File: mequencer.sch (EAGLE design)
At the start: 75 parts, among them IC1 NE555D, IC10 LF353D, IC11 NE555D, IC12 NE555D, IC2 4163D, IC3 74HC85D, IC4 4051D, IC5 4051D, IC6 74HCT04D, IC7 4051D, IC8 4051D, IC9 LF353D, U1 74LVC1G08SE-7

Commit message: Moving shit around more
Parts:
- removed C20, C21, C22, C23, C24, C25: .1uF, SparkFun-Capacitors:CAP0603-CAP
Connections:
- net 5V: no longer C20.2, C21.2, C22.2, C23.2, C24.2, C25.2
- net N$7: no longer C20.1, C21.1, C22.1, C23.1, C24.1, C25.1
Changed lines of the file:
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@@
 <part name="C18" library="SparkFun-Capacitors" deviceset="CAP" device="0603-CAP" value=".1uF"/>
 <part name="C19" library="SparkFun-Capacitors" deviceset="CAP" device="0603-CAP" value=".1uF"/>
-<part name="C20" library="SparkFun-Capacitors" deviceset="CAP" device="0603-CAP" value=".1uF"/>
-<part name="C21" library="SparkFun-Capacitors" deviceset="CAP" device="0603-CAP" value=".1uF"/>
-<part name="C22" library="SparkFun-Capacitors" deviceset="CAP" device="0603-CAP" value=".1uF"/>
-<part name="C23" library="SparkFun-Capacitors" deviceset="CAP" device="0603-CAP" value=".1uF"/>
-<part name="C24" library="SparkFun-Capacitors" deviceset="CAP" device="0603-CAP" value=".1uF"/>
-<part name="C25" library="SparkFun-Capacitors" deviceset="CAP" device="0603-CAP" value=".1uF"/>
 <part name="R2" library="SparkFun-Resistors" deviceset="RESISTOR" device="0603" value="1k"/>
 <part name="JP2" library="SparkFun-Connectors" deviceset="M04" device="JST-PTH"/>
@@
 <instance part="C5" gate="G$1" x="26.67" y="173.99" rot="R180"/>
 <instance part="C6" gate="G$1" x="55.88" y="172.72" rot="R180"/>
-<instance part="SUPPLY13" gate="G$1" x="92.71" y="181.61"/>
+<instance part="SUPPLY13" gate="G$1" x="128.27" y="184.15"/>
 <instance part="GND4" gate="1" x="237.49" y="100.33"/>
 <instance part="C7" gate="G$1" x="156.21" y="180.34" rot="R180"/>
@@
 <instance part="C18" gate="G$1" x="135.89" y="180.34" rot="R180"/>
 <instance part="C19" gate="G$1" x="130.81" y="180.34" rot="R180"/>
-<instance part="C20" gate="G$1" x="125.73" y="180.34" rot="R180"/>
-<instance part="C21" gate="G$1" x="120.65" y="180.34" rot="R180"/>
-<instance part="C22" gate="G$1" x="115.57" y="180.34" rot="R180"/>
-<instance part="C23" gate="G$1" x="110.49" y="180.34" rot="R180"/>
-<instance part="C24" gate="G$1" x="105.41" y="180.34" rot="R180"/>
-<instance part="C25" gate="G$1" x="100.33" y="180.34" rot="R180"/>
 <instance part="R2" gate="G$1" x="25.4" y="149.86"/>
 <instance part="JP2" gate="G$1" x="10.16" y="-15.24"/>
@@
 </segment>
 <segment>
-<pinref part="C25" gate="G$1" pin="2"/>
-<pinref part="C24" gate="G$1" pin="2"/>
-<wire x1="100.33" y1="182.88" x2="105.41" y2="182.88" width="0.1524" layer="91"/>
-<pinref part="C23" gate="G$1" pin="2"/>
-<wire x1="105.41" y1="182.88" x2="110.49" y2="182.88" width="0.1524" layer="91"/>
-<junction x="105.41" y="182.88"/>
-<pinref part="C22" gate="G$1" pin="2"/>
-<wire x1="110.49" y1="182.88" x2="115.57" y2="182.88" width="0.1524" layer="91"/>
-<junction x="110.49" y="182.88"/>
-<pinref part="C21" gate="G$1" pin="2"/>
-<wire x1="115.57" y1="182.88" x2="120.65" y2="182.88" width="0.1524" layer="91"/>
-<junction x="115.57" y="182.88"/>
-<pinref part="C20" gate="G$1" pin="2"/>
-<wire x1="120.65" y1="182.88" x2="125.73" y2="182.88" width="0.1524" layer="91"/>
-<junction x="120.65" y="182.88"/>
 <pinref part="C19" gate="G$1" pin="2"/>
-<wire x1="125.73" y1="182.88" x2="130.81" y2="182.88" width="0.1524" layer="91"/>
-<junction x="125.73" y="182.88"/>
+<wire x1="128.27" y1="182.88" x2="130.81" y2="182.88" width="0.1524" layer="91"/>
 <pinref part="C18" gate="G$1" pin="2"/>
 <wire x1="130.81" y1="182.88" x2="135.89" y2="182.88" width="0.1524" layer="91"/>
@@
 <junction x="186.69" y="182.88"/>
 <pinref part="SUPPLY13" gate="G$1" pin="5V"/>
-<wire x1="100.33" y1="182.88" x2="92.71" y2="182.88" width="0.1524" layer="91"/>
-<wire x1="92.71" y1="182.88" x2="92.71" y2="181.61" width="0.1524" layer="91"/>
-<junction x="100.33" y="182.88"/>
+<wire x1="128.27" y1="182.88" x2="128.27" y2="184.15" width="0.1524" layer="91"/>
 </segment>
 <segment>
@@
 <wire x1="208.28" y1="124.46" x2="223.52" y2="124.46" width="0.1524" layer="91"/>
 <junction x="223.52" y="124.46"/>
-<pinref part="C25" gate="G$1" pin="1"/>
-<pinref part="C24" gate="G$1" pin="1"/>
-<wire x1="100.33" y1="175.26" x2="105.41" y2="175.26" width="0.1524" layer="91"/>
-<pinref part="C23" gate="G$1" pin="1"/>
-<wire x1="105.41" y1="175.26" x2="110.49" y2="175.26" width="0.1524" layer="91"/>
-<junction x="105.41" y="175.26"/>
-<pinref part="C22" gate="G$1" pin="1"/>
-<wire x1="110.49" y1="175.26" x2="115.57" y2="175.26" width="0.1524" layer="91"/>
-<junction x="110.49" y="175.26"/>
-<pinref part="C21" gate="G$1" pin="1"/>
-<wire x1="115.57" y1="175.26" x2="120.65" y2="175.26" width="0.1524" layer="91"/>
-<junction x="115.57" y="175.26"/>
-<pinref part="C20" gate="G$1" pin="1"/>
-<wire x1="120.65" y1="175.26" x2="125.73" y2="175.26" width="0.1524" layer="91"/>
-<junction x="120.65" y="175.26"/>
 <pinref part="C19" gate="G$1" pin="1"/>
-<wire x1="125.73" y1="175.26" x2="130.81" y2="175.26" width="0.1524" layer="91"/>
-<junction x="125.73" y="175.26"/>
 <pinref part="C18" gate="G$1" pin="1"/>
 <wire x1="130.81" y1="175.26" x2="135.89" y2="175.26" width="0.1524" layer="91"/>
-<junction x="130.81" y="175.26"/>
 <pinref part="C17" gate="G$1" pin="1"/>
 <wire x1="135.89" y1="175.26" x2="140.97" y2="175.26" width="0.1524" layer="91"/>

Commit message: stuff
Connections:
- removed net N$7: C10.1, C11.1, C12.1, C13.1, C14.1, C15.1, C16.1, C17.1, C18.1, C19.1, C7.1, C8.1, C9.1, IC10P.V+, IC2P.VDD, IC3P.VCC, IC4P.VCC, IC5P.VCC, IC6P.VCC, IC7P.VCC, IC8P.VCC, IC9P.V+
- net 5V: now also IC10P.V+, IC2P.VDD, IC3P.VCC, IC4P.VCC, IC5P.VCC, IC6P.VCC, IC7P.VCC, IC8P.VCC, IC9P.V+
- net GND: now also C10.1, C11.1, C12.1, C13.1, C14.1, C15.1, C16.1, C17.1, C18.1, C19.1, C7.1, C8.1, C9.1
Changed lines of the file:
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@@
 <setting verticaltext="up"/>
 </settings>
-<grid distance="0.1" unitdist="inch" unit="inch" style="lines" multiple="1" display="no" altdistance="0.01" altunitdist="inch" altunit="inch"/>
+<grid distance="0.05" unitdist="inch" unit="inch" style="lines" multiple="1" display="yes" altdistance="0.005" altunitdist="inch" altunit="inch"/>
 <layers>
 <layer number="1" name="Top" color="4" fill="1" visible="no" active="no"/>
@@
 <part name="SUPPLY29" library="SparkFun-Aesthetics" deviceset="5V" device=""/>
 <part name="GND3" library="SparkFun-Aesthetics" deviceset="GND" device=""/>
+<part name="GND5" library="SparkFun-Aesthetics" deviceset="GND" device=""/>
+<part name="SUPPLY4" library="SparkFun-Aesthetics" deviceset="5V" device=""/>
 </parts>
 <sheets>
@@
 <instance part="SUPPLY29" gate="G$1" x="78.74" y="114.3"/>
 <instance part="GND3" gate="1" x="101.6" y="88.9"/>
+<instance part="GND5" gate="1" x="191.77" y="171.45"/>
+<instance part="SUPPLY4" gate="G$1" x="208.28" y="177.8"/>
 </instances>
 <busses>
@@
 <pinref part="SUPPLY29" gate="G$1" pin="5V"/>
 </segment>
+<segment>
+<pinref part="IC8" gate="P" pin="VCC"/>
+<pinref part="IC10" gate="P" pin="V+"/>
+<wire x1="233.68" y1="124.46" x2="223.52" y2="124.46" width="0.1524" layer="91"/>
+<wire x1="208.28" y1="124.46" x2="223.52" y2="124.46" width="0.1524" layer="91"/>
+<junction x="223.52" y="124.46"/>
+<pinref part="IC9" gate="P" pin="V+"/>
+<wire x1="208.28" y1="177.8" x2="215.9" y2="177.8" width="0.1524" layer="91"/>
+<pinref part="IC3" gate="P" pin="VCC"/>
+<wire x1="226.06" y1="177.8" x2="215.9" y2="177.8" width="0.1524" layer="91"/>
+<junction x="215.9" y="177.8"/>
+<pinref part="IC2" gate="P" pin="VDD"/>
+<wire x1="226.06" y1="177.8" x2="233.68" y2="177.8" width="0.1524" layer="91"/>
+<junction x="226.06" y="177.8"/>
+<pinref part="IC4" gate="P" pin="VCC"/>
+<pinref part="IC5" gate="P" pin="VCC"/>
+<wire x1="233.68" y1="160.02" x2="220.98" y2="160.02" width="0.1524" layer="91"/>
+<wire x1="220.98" y1="160.02" x2="208.28" y2="160.02" width="0.1524" layer="91"/>
+<junction x="220.98" y="160.02"/>
+<wire x1="208.28" y1="177.8" x2="208.28" y2="160.02" width="0.1524" layer="91"/>
+<pinref part="IC6" gate="P" pin="VCC"/>
+<pinref part="IC7" gate="P" pin="VCC"/>
+<wire x1="233.68" y1="142.24" x2="226.06" y2="142.24" width="0.1524" layer="91"/>
+<wire x1="226.06" y1="142.24" x2="208.28" y2="142.24" width="0.1524" layer="91"/>
+<junction x="226.06" y="142.24"/>
+<wire x1="208.28" y1="160.02" x2="208.28" y2="142.24" width="0.1524" layer="91"/>
+<junction x="208.28" y="160.02"/>
+<wire x1="208.28" y1="124.46" x2="208.28" y2="142.24" width="0.1524" layer="91"/>
+<junction x="208.28" y="142.24"/>
+<pinref part="SUPPLY4" gate="G$1" pin="5V"/>
+<junction x="208.28" y="177.8"/>
+</segment>
 </net>
 <net name="GND" class="0">
@@
 <wire x1="101.6" y1="91.44" x2="96.52" y2="91.44" width="0.1524" layer="91"/>
 </segment>
+<segment>
+<pinref part="C16" gate="G$1" pin="1"/>
+<pinref part="C15" gate="G$1" pin="1"/>
+<wire x1="186.69" y1="175.26" x2="191.77" y2="175.26" width="0.1524" layer="91"/>
+<junction x="186.69" y="175.26"/>
+<pinref part="C14" gate="G$1" pin="1"/>
+<wire x1="181.61" y1="175.26" x2="186.69" y2="175.26" width="0.1524" layer="91"/>
+<junction x="181.61" y="175.26"/>
+<pinref part="C11" gate="G$1" pin="1"/>
+<wire x1="176.53" y1="175.26" x2="181.61" y2="175.26" width="0.1524" layer="91"/>
+<junction x="176.53" y="175.26"/>
+<pinref part="C10" gate="G$1" pin="1"/>
+<wire x1="171.45" y1="175.26" x2="176.53" y2="175.26" width="0.1524" layer="91"/>
+<junction x="171.45" y="175.26"/>
+<pinref part="C9" gate="G$1" pin="1"/>
+<wire x1="166.37" y1="175.26" x2="171.45" y2="175.26" width="0.1524" layer="91"/>
+<junction x="166.37" y="175.26"/>
+<pinref part="C8" gate="G$1" pin="1"/>
+<wire x1="161.29" y1="175.26" x2="166.37" y2="175.26" width="0.1524" layer="91"/>
+<junction x="161.29" y="175.26"/>
+<pinref part="C7" gate="G$1" pin="1"/>
+<wire x1="156.21" y1="175.26" x2="161.29" y2="175.26" width="0.1524" layer="91"/>
+<junction x="156.21" y="175.26"/>
+<pinref part="C12" gate="G$1" pin="1"/>
+<wire x1="151.13" y1="175.26" x2="156.21" y2="175.26" width="0.1524" layer="91"/>
+<junction x="151.13" y="175.26"/>
+<pinref part="C13" gate="G$1" pin="1"/>
+<wire x1="146.05" y1="175.26" x2="151.13" y2="175.26" width="0.1524" layer="91"/>
+<junction x="146.05" y="175.26"/>
+<pinref part="C17" gate="G$1" pin="1"/>
+<wire x1="140.97" y1="175.26" x2="146.05" y2="175.26" width="0.1524" layer="91"/>
+<junction x="140.97" y="175.26"/>
+<pinref part="C18" gate="G$1" pin="1"/>
+<wire x1="135.89" y1="175.26" x2="140.97" y2="175.26" width="0.1524" layer="91"/>
+<junction x="135.89" y="175.26"/>
+<pinref part="C19" gate="G$1" pin="1"/>
+<wire x1="130.81" y1="175.26" x2="135.89" y2="175.26" width="0.1524" layer="91"/>
+<pinref part="GND5" gate="1" pin="GND"/>
+<wire x1="191.77" y1="175.26" x2="191.77" y2="173.99" width="0.2032" layer="91"/>
+</segment>
 </net>
 <net name="N$2" class="0">
@@
 </segment>
 </net>
-<net name="N$7" class="0">
-<segment>
-<pinref part="IC8" gate="P" pin="VCC"/>
-<pinref part="IC10" gate="P" pin="V+"/>
-<wire x1="233.68" y1="124.46" x2="223.52" y2="124.46" width="0.1524" layer="91"/>
-<wire x1="208.28" y1="124.46" x2="223.52" y2="124.46" width="0.1524" layer="91"/>
-<junction x="223.52" y="124.46"/>
-<pinref part="C19" gate="G$1" pin="1"/>
-<pinref part="C18" gate="G$1" pin="1"/>
-<wire x1="130.81" y1="175.26" x2="135.89" y2="175.26" width="0.1524" layer="91"/>
-<pinref part="C17" gate="G$1" pin="1"/>
-<wire x1="135.89" y1="175.26" x2="140.97" y2="175.26" width="0.1524" layer="91"/>
-<junction x="135.89" y="175.26"/>
-<pinref part="C13" gate="G$1" pin="1"/>
-<wire x1="140.97" y1="175.26" x2="146.05" y2="175.26" width="0.1524" layer="91"/>
-<junction x="140.97" y="175.26"/>
-<pinref part="C12" gate="G$1" pin="1"/>
-<wire x1="146.05" y1="175.26" x2="151.13" y2="175.26" width="0.1524" layer="91"/>
-<junction x="146.05" y="175.26"/>
-<pinref part="C7" gate="G$1" pin="1"/>
-<wire x1="151.13" y1="175.26" x2="156.21" y2="175.26" width="0.1524" layer="91"/>
-<junction x="151.13" y="175.26"/>
-<pinref part="C8" gate="G$1" pin="1"/>
-<wire x1="156.21" y1="175.26" x2="161.29" y2="175.26" width="0.1524" layer="91"/>
-<junction x="156.21" y="175.26"/>
-<pinref part="C9" gate="G$1" pin="1"/>
-<wire x1="161.29" y1="175.26" x2="166.37" y2="175.26" width="0.1524" layer="91"/>
-<junction x="161.29" y="175.26"/>
-<pinref part="C10" gate="G$1" pin="1"/>
-<wire x1="166.37" y1="175.26" x2="171.45" y2="175.26" width="0.1524" layer="91"/>
-<junction x="166.37" y="175.26"/>
-<pinref part="C11" gate="G$1" pin="1"/>
-<wire x1="171.45" y1="175.26" x2="176.53" y2="175.26" width="0.1524" layer="91"/>
-<junction x="171.45" y="175.26"/>
-<pinref part="C14" gate="G$1" pin="1"/>
-<wire x1="176.53" y1="175.26" x2="181.61" y2="175.26" width="0.1524" layer="91"/>
-<junction x="176.53" y="175.26"/>
-<pinref part="C15" gate="G$1" pin="1"/>
-<wire x1="181.61" y1="175.26" x2="186.69" y2="175.26" width="0.1524" layer="91"/>
-<junction x="181.61" y="175.26"/>
-<pinref part="C16" gate="G$1" pin="1"/>
-<wire x1="186.69" y1="175.26" x2="191.77" y2="175.26" width="0.1524" layer="91"/>
-<junction x="186.69" y="175.26"/>
-<junction x="191.77" y="175.26"/>
-<wire x1="191.77" y1="175.26" x2="208.28" y2="175.26" width="0.1524" layer="91"/>
-<wire x1="208.28" y1="175.26" x2="208.28" y2="177.8" width="0.1524" layer="91"/>
-<pinref part="IC9" gate="P" pin="V+"/>
-<wire x1="208.28" y1="177.8" x2="215.9" y2="177.8" width="0.1524" layer="91"/>
-<pinref part="IC3" gate="P" pin="VCC"/>
-<wire x1="226.06" y1="177.8" x2="215.9" y2="177.8" width="0.1524" layer="91"/>
-<junction x="215.9" y="177.8"/>
-<pinref part="IC2" gate="P" pin="VDD"/>
-<wire x1="226.06" y1="177.8" x2="233.68" y2="177.8" width="0.1524" layer="91"/>
-<junction x="226.06" y="177.8"/>
-<pinref part="IC4" gate="P" pin="VCC"/>
-<pinref part="IC5" gate="P" pin="VCC"/>
-<wire x1="233.68" y1="160.02" x2="220.98" y2="160.02" width="0.1524" layer="91"/>
-<wire x1="220.98" y1="160.02" x2="208.28" y2="160.02" width="0.1524" layer="91"/>
-<junction x="220.98" y="160.02"/>
-<wire x1="208.28" y1="175.26" x2="208.28" y2="160.02" width="0.1524" layer="91"/>
-<junction x="208.28" y="175.26"/>
-<pinref part="IC6" gate="P" pin="VCC"/>
-<pinref part="IC7" gate="P" pin="VCC"/>
-<wire x1="233.68" y1="142.24" x2="226.06" y2="142.24" width="0.1524" layer="91"/>
-<wire x1="226.06" y1="142.24" x2="208.28" y2="142.24" width="0.1524" layer="91"/>
-<junction x="226.06" y="142.24"/>
-<wire x1="208.28" y1="160.02" x2="208.28" y2="142.24" width="0.1524" layer="91"/>
-<junction x="208.28" y="160.02"/>
-<wire x1="208.28" y1="124.46" x2="208.28" y2="142.24" width="0.1524" layer="91"/>
-<junction x="208.28" y="142.24"/>
-</segment>
-</net>

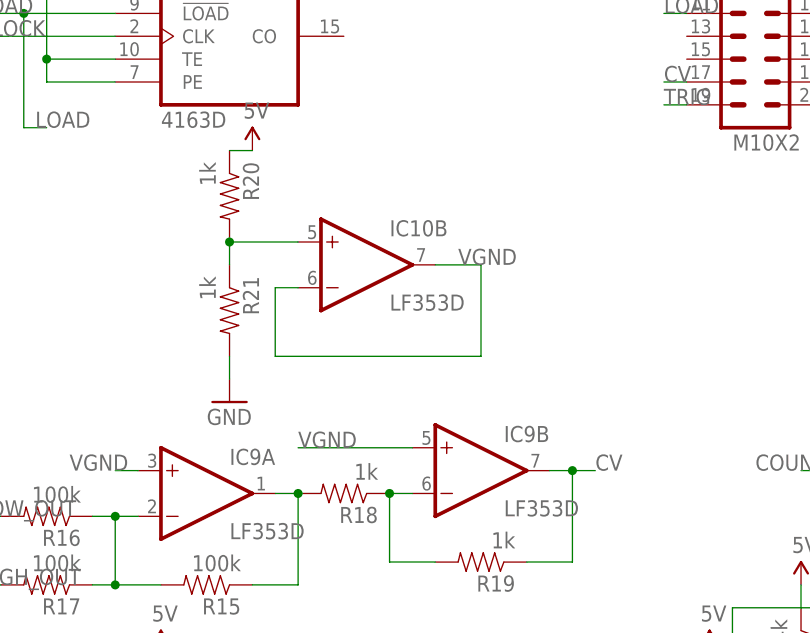
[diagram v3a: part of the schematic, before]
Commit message: changed some 1ks to 100ks to draw less current
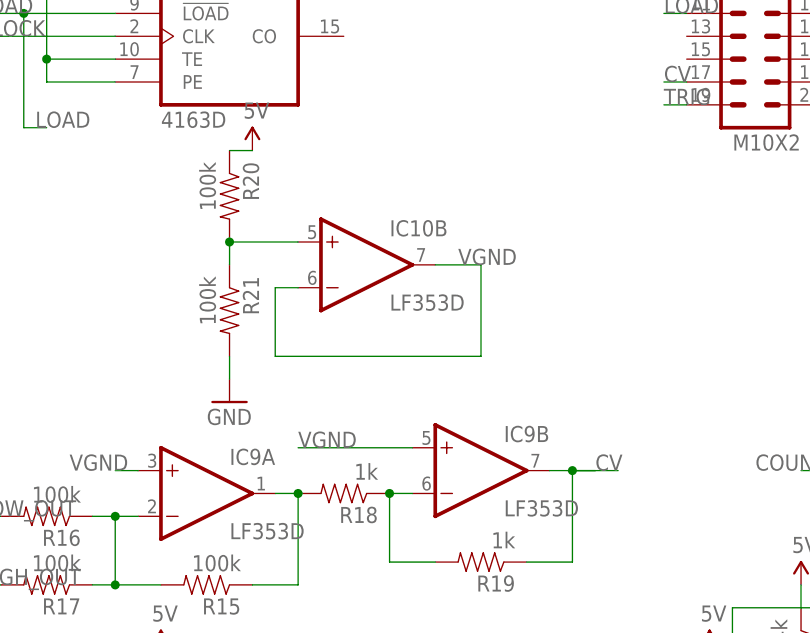
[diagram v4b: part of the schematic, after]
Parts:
- R20, R21: value 1k -> 100k
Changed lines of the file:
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@@
 <part name="R19" library="SparkFun-Resistors" deviceset="RESISTOR" device="0603" value="1k"/>
 <part name="IC10" library="linear" deviceset="LF353" device="D"/>
-<part name="R20" library="SparkFun-Resistors" deviceset="RESISTOR" device="0603" value="1k"/>
-<part name="R21" library="SparkFun-Resistors" deviceset="RESISTOR" device="0603" value="1k"/>
+<part name="R20" library="SparkFun-Resistors" deviceset="RESISTOR" device="0603" value="100k"/>
+<part name="R21" library="SparkFun-Resistors" deviceset="RESISTOR" device="0603" value="100k"/>
 <part name="GND10" library="SparkFun-Aesthetics" deviceset="GND" device=""/>
 <part name="SUPPLY7" library="SparkFun-Aesthetics" deviceset="5V" device=""/>
@@
 <junction x="68.58" y="50.8"/>
 <label x="71.12" y="50.8" size="1.778" layer="95"/>
-</segment>
-<segment>
+<wire x1="73.66" y1="50.8" x2="68.58" y2="50.8" width="0.1524" layer="91"/>
+</segment>
+<segment>

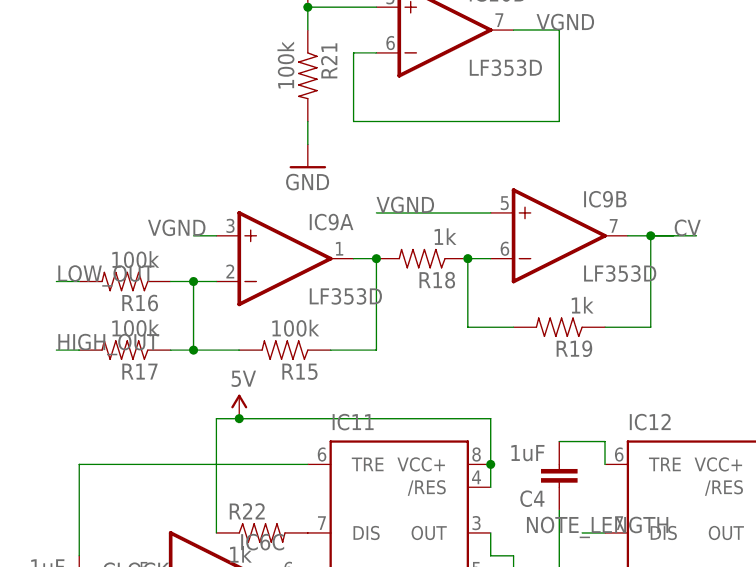
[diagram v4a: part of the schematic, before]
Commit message: bumped the resistance values in the CV summer so that the resistance in note pot won't affect the note's CV when it is in rest mode
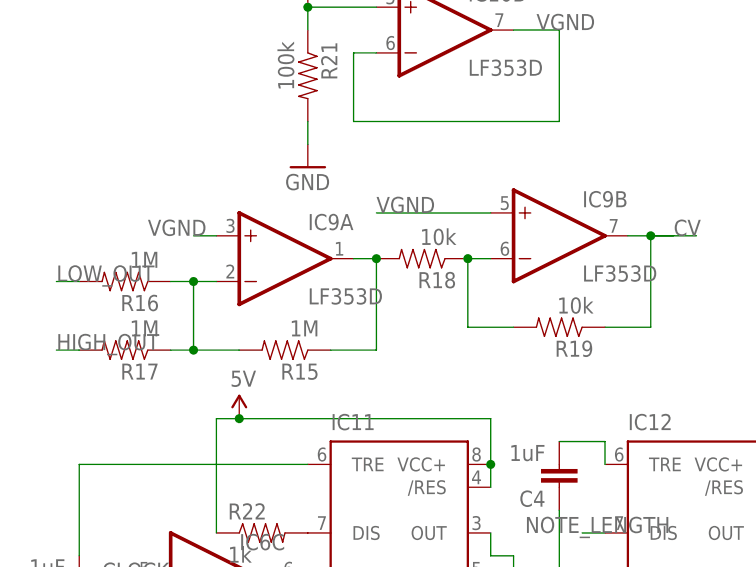
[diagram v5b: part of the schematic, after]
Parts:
- R15, R16, R17: value 100k -> 1M
- R18, R19: value 1k -> 10k
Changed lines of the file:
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@@
 <part name="R14" library="SparkFun-Resistors" deviceset="RESISTOR" device="0603"/>
 <part name="IC9" library="linear" deviceset="LF353" device="D"/>
-<part name="R15" library="SparkFun-Resistors" deviceset="RESISTOR" device="0603" value="100k"/>
-<part name="R16" library="SparkFun-Resistors" deviceset="RESISTOR" device="0603" value="100k"/>
-<part name="R17" library="SparkFun-Resistors" deviceset="RESISTOR" device="0603" value="100k"/>
-<part name="R18" library="SparkFun-Resistors" deviceset="RESISTOR" device="0603" value="1k"/>
-<part name="R19" library="SparkFun-Resistors" deviceset="RESISTOR" device="0603" value="1k"/>
+<part name="R15" library="SparkFun-Resistors" deviceset="RESISTOR" device="0603" value="1M"/>
+<part name="R16" library="SparkFun-Resistors" deviceset="RESISTOR" device="0603" value="1M"/>
+<part name="R17" library="SparkFun-Resistors" deviceset="RESISTOR" device="0603" value="1M"/>
+<part name="R18" library="SparkFun-Resistors" deviceset="RESISTOR" device="0603" value="10k"/>
+<part name="R19" library="SparkFun-Resistors" deviceset="RESISTOR" device="0603" value="10k"/>
 <part name="IC10" library="linear" deviceset="LF353" device="D"/>
 <part name="R20" library="SparkFun-Resistors" deviceset="RESISTOR" device="0603" value="100k"/>
